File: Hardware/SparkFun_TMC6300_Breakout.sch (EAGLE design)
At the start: 31 parts, among them U2 TMC6300

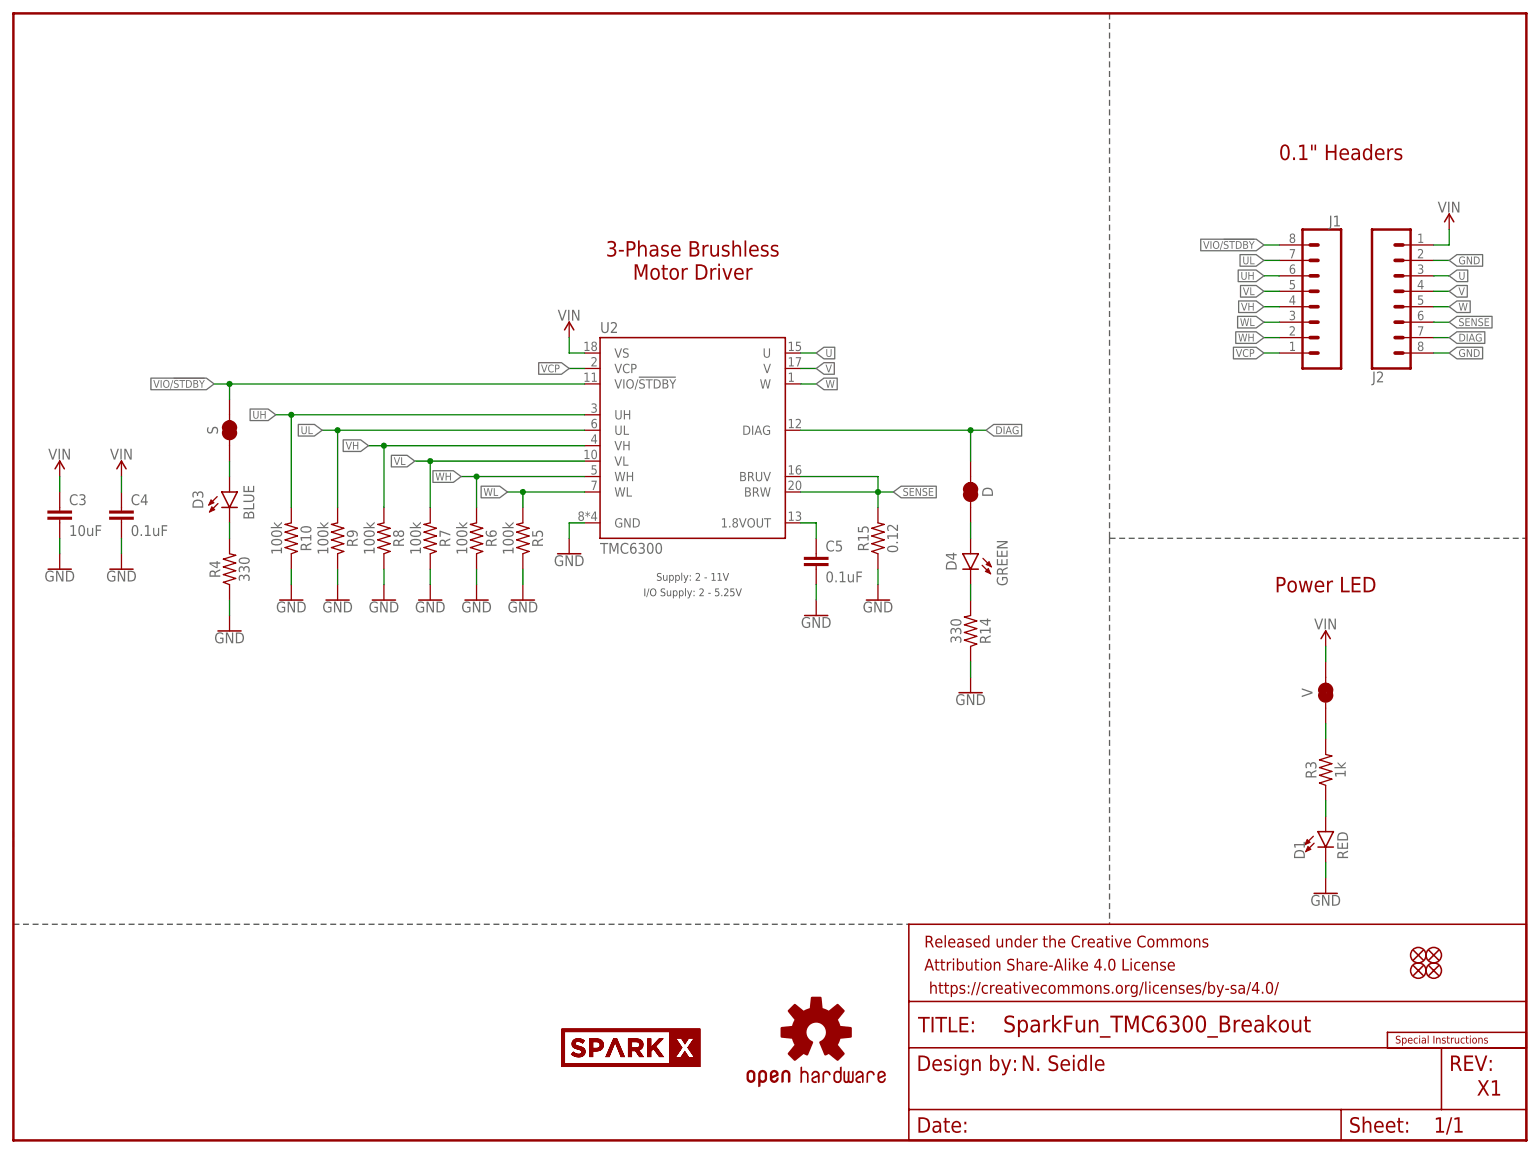
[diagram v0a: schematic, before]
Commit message: Updates for red review
Added SparkFun logo, updated notes in schematic for user, changed blue LED resistor value, added OSHW logo, created panel and CAM files.
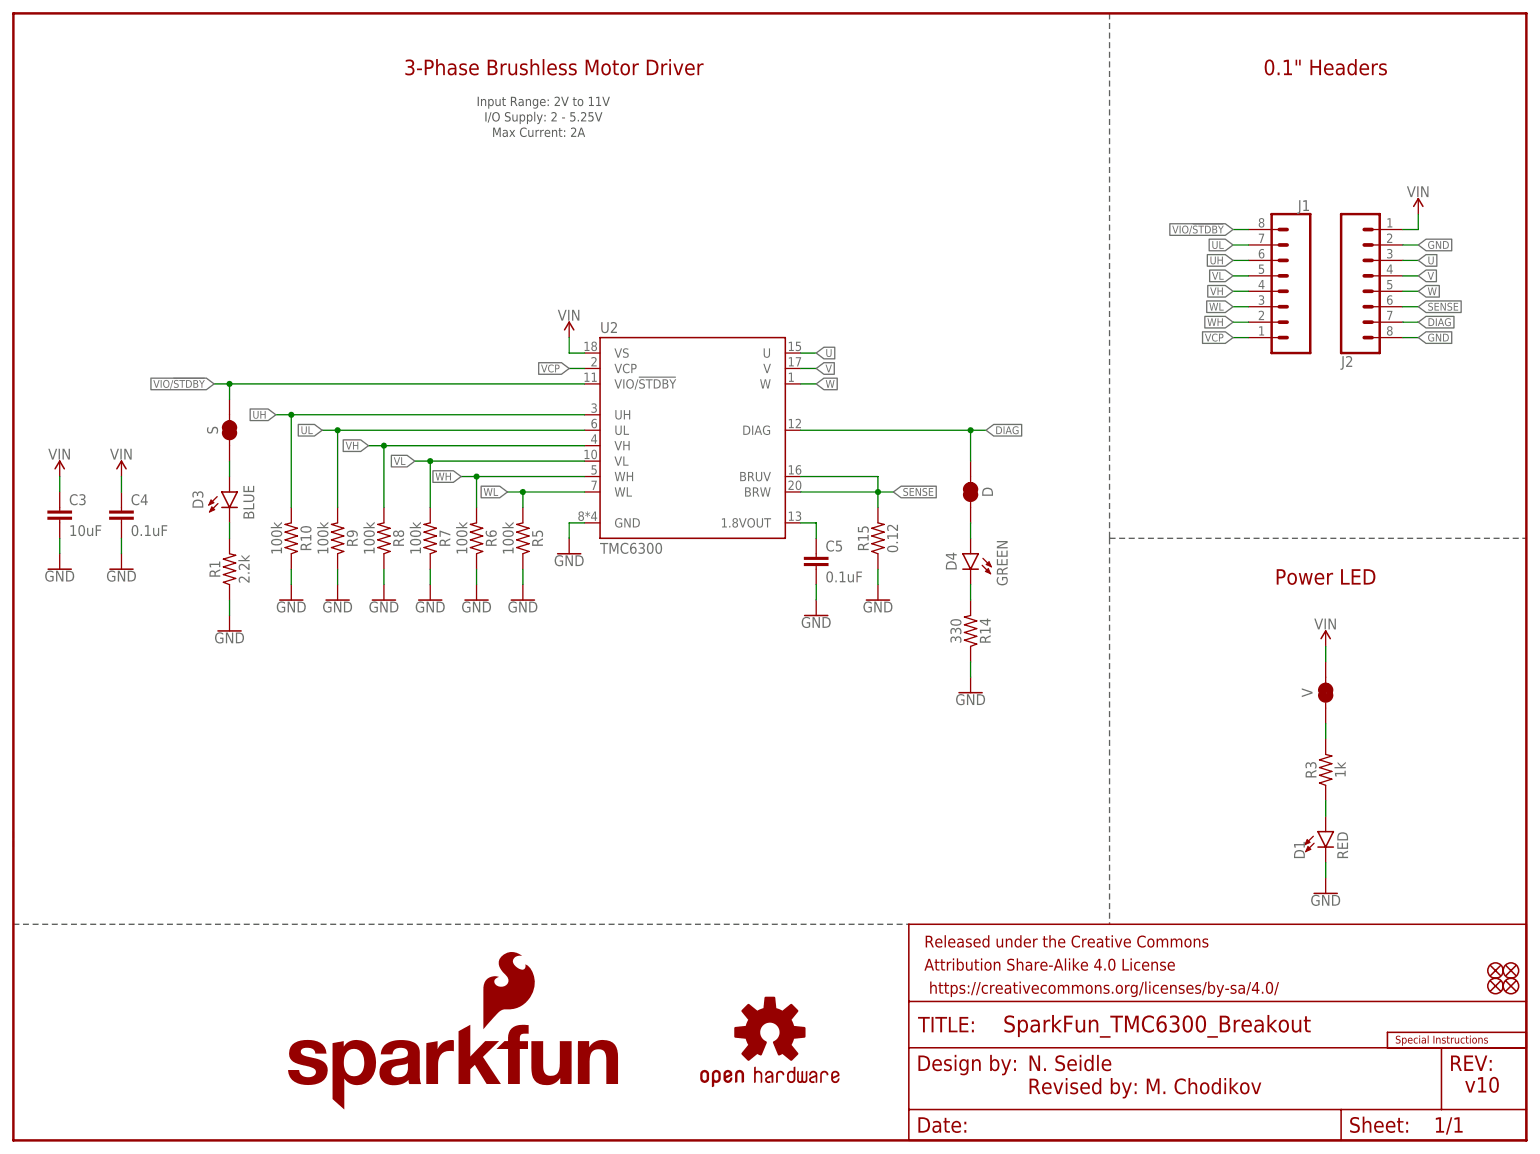
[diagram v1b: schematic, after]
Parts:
- removed LOGO1: OSHW-LOGONO_SILK, SparkFun-Aesthetics:OSHW-LOGONO_SILK
- removed R4: 330, SparkFun-Resistors:330OHM-0603-1/10W-1%
- removed U$36, U$37: SPARKX-LOGO2, SparkX:SPARKX-LOGO2
- added LOGO3: SFE_LOGO_NAME.1_INCH, SparkFun-Aesthetics:SFE_LOGO_NAME.1_INCH
- added LOGO4: SFE_LOGO_FLAME.1_INCH, SparkFun-Aesthetics:SFE_LOGO_FLAME.1_INCH
- added LOGO5: OSHW-LOGOS, SparkFun-Aesthetics:OSHW-LOGOS
- added R1: 2.2k, SparkFun-Resistors:2.2KOHM-0603-1/10W-1%
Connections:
- net GND: now also R1.1; no longer R4.1
- net N$10: now also R1.2; no longer R4.2
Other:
- note added: "Input Range: 2V to 11V"
- note added: "Max Current: 2A"
- note added: "Revised by: M. Chodikov"
- note added: "v10"
- note removed: "Supply: 2 - 11V"
- note removed: "X1"
- moved on the sheet: J1, J2

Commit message: Changes made from design notes
Changed vias to be all the same size, added paragraphs to S and D jumpers to explain what they're going to, added tRestrict layer to remove natural jumper between GND pads, fixed acid trap, added more GND vias for better heat sinking.
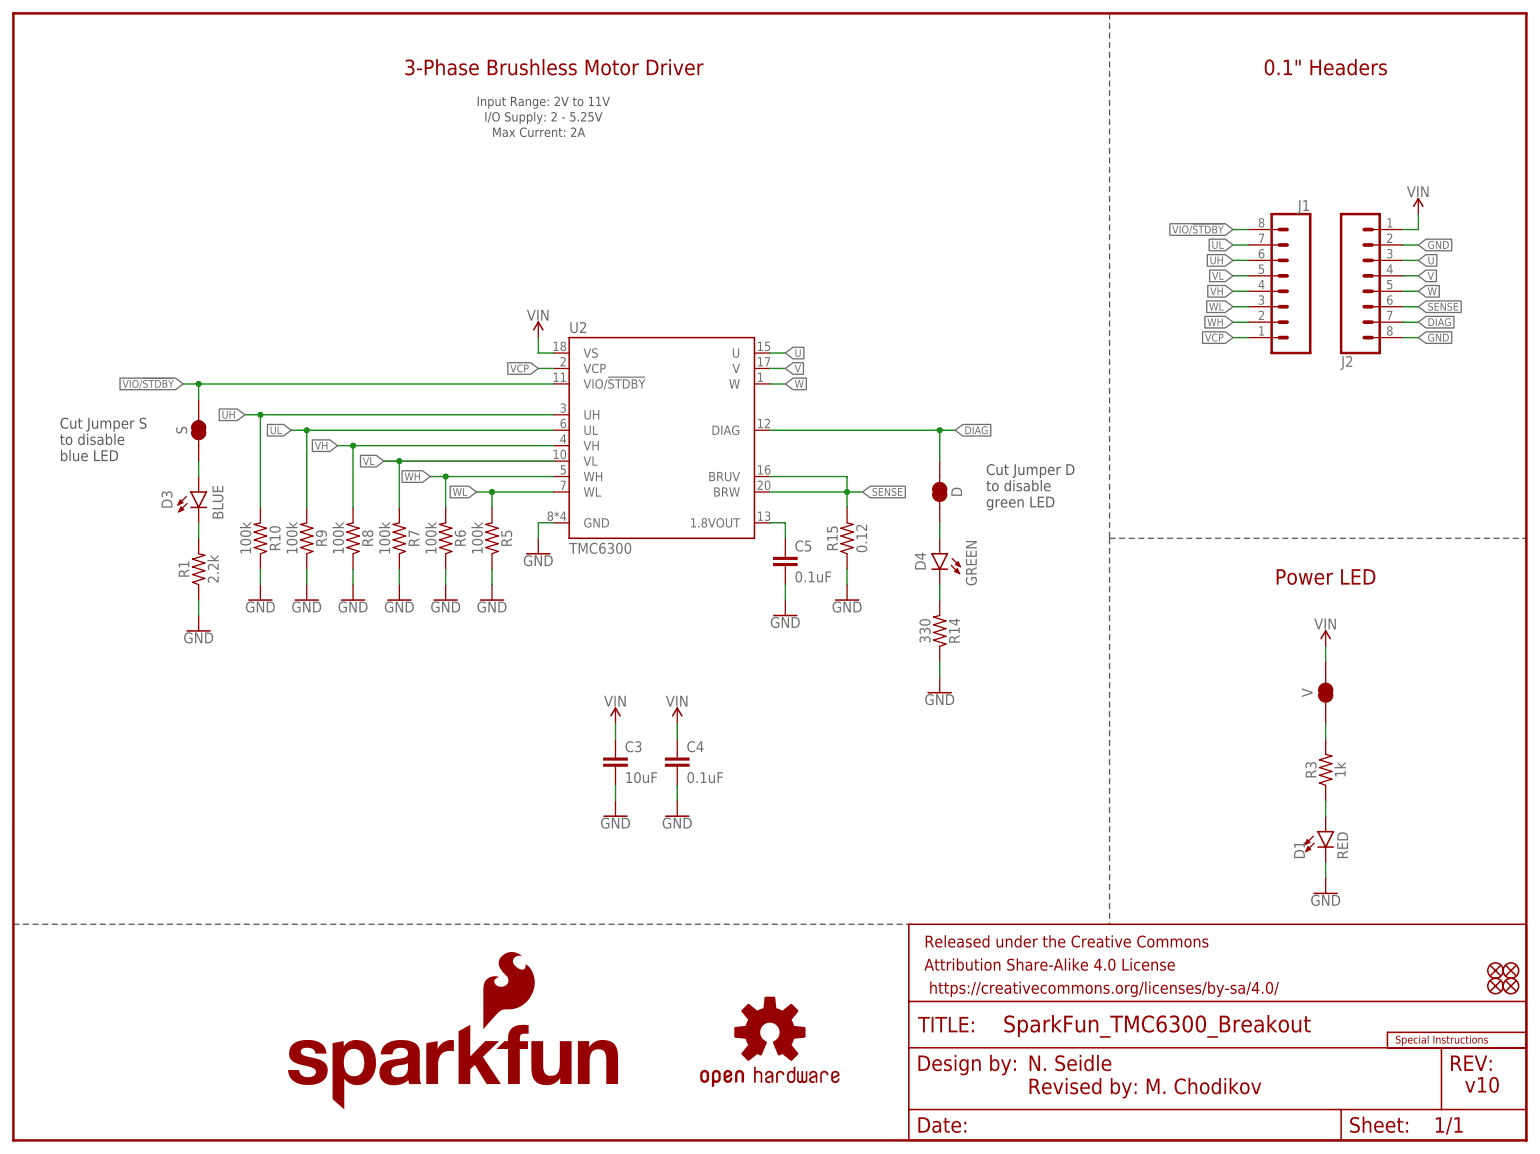
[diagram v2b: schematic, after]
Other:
- note added: "Cut Jumper D to disable green LED"
- note added: "Cut Jumper S to disable blue LED"
- moved on the sheet: C3, C4, C5, D, D3, D4, R1, R10, R14, R15, R5, R6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

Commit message: Updates from design review
Changed tCream on the TMC6300 to be reduced by 5%, changed tRestrict polygon to a rectangle, adjusted C5 to match the datasheet for a good return path, adjusted some routing for less acid traps, adjusted ratio of numbers on layers from 15% to 18%, and created a smaller SparkFun logo to fit better on the top side of the board - not 0.08 instead of 0.1
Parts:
- LOGO3: value SFE_LOGO_NAME.1_INCH -> SFE_LOGO_NAME.08_INCH; device SparkFun-Aesthetics:SFE_LOGO_NAME.1_INCH -> SparkFun-Aesthetics:SFE_LOGO_NAME.08_INCH
- renumbered U2 to U1
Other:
- note added: "Cut Jumper D to disable diagnostic LED"
- note added: "Cut Jumper S to disable standby LED"
- note removed: "Cut Jumper D to disable green LED"
- note removed: "Cut Jumper S to disable blue LED"

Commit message: Final updates before ordering
Adjusted GND traces from TMC6300 for better connection, added paragraph for Power LED in schematic, updated panelized files for ordering.
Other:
- note added: "Cut Jumper V to disable power LED"
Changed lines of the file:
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@@
 to disable
 diagnostic LED</text>
+<text x="223.52" y="71.12" size="1.778" layer="97" font="vector">Cut Jumper V
+to disable
+power LED</text>
 </plain>
 <instances>
